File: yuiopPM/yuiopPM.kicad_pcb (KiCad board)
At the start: 2 copper layers, 17.8 x 33 mm, 19 parts, among them J1 USB_B_Micro, J2 Conn_01x12, J3 Conn_01x12, U1 ATmega32U4-AU, X1 16MHz

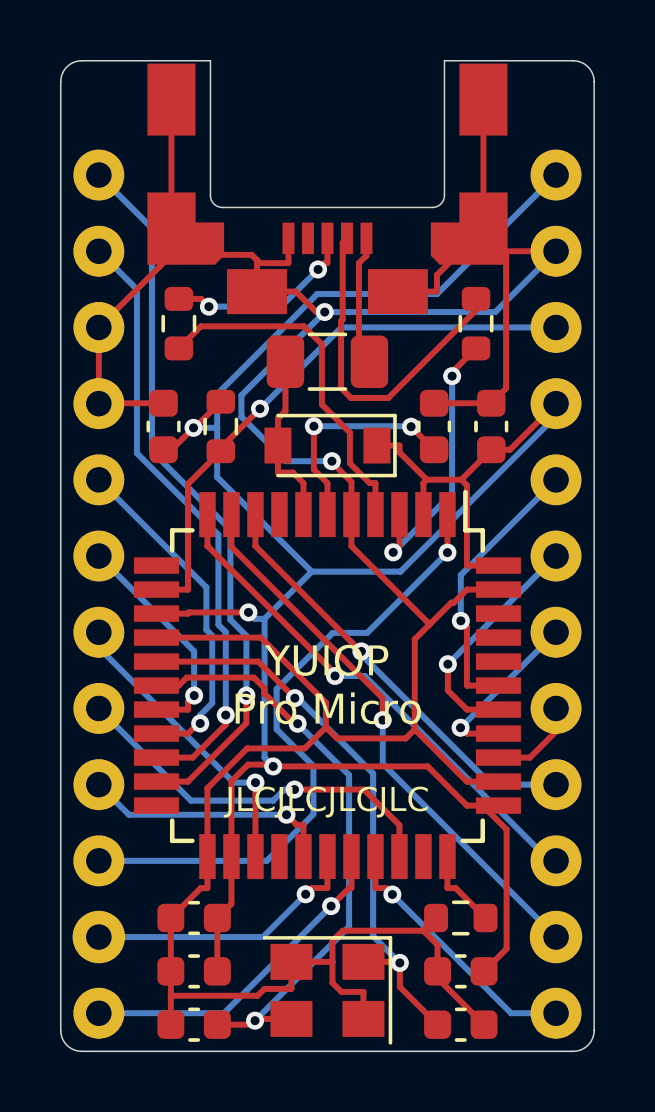
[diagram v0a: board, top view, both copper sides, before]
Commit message: fix footprints after yuiop31rs production
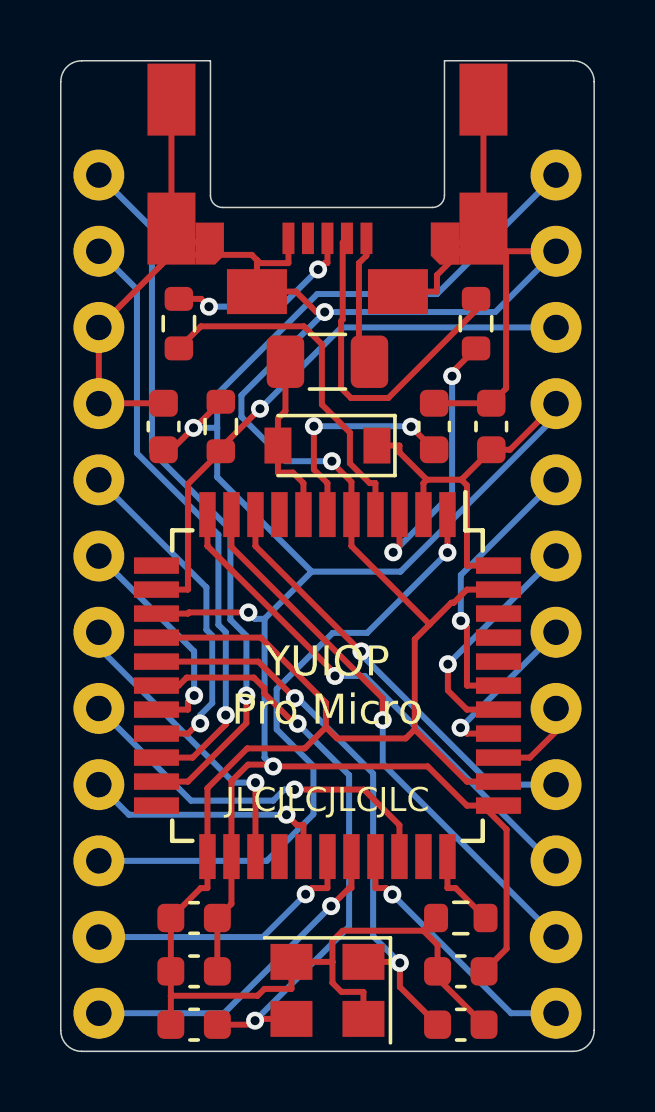
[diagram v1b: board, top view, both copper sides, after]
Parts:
- J1: footprint KeyboardController:USB-MicroB_ZX62M-B-5P -> KeyboardController:USB-MicroB_ZX62M-B-5P_v2
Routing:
- net /GND: track 115.1 -> 118.0 mm
